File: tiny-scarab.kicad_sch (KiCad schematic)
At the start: 22 parts, among them J1 Conn_02x07_Odd_Even, J2 Conn_01x05_Pin, J4 Conn_02x07_Odd_Even, J5 Screw_Hole, J6 Screw_Hole, J7 Screw_Hole, J8 Screw_Hole, Q3 IRLML2502TRPBF, SW4 SLW-883935-2A-D, SW5 PTS636_SL43_SMTR_LFS, U1 CH32V003F4P6

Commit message: Improve layout
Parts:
- removed J2: Conn_01x05_Pin, Connector_PinHeader_2.54mm:PinHeader_1x05_P2.54mm_Vertical, symbol Connector:Conn_01x05_Pin
- added J2: Conn_01x05_Pin, Tiny_Scarab:PinHeader_1x05_P2.54mm_Vertical, symbol Tiny_Scarab:Conn_01x05_Pin
- Q3: footprint Package_TO_SOT_SMD:SOT-23 -> Tiny_Scarab:SOT-23
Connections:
- net +3V3: now also J2.2 (Pin_2)
- net GND: now also J2.1 (Pin_1)
- net RST_IN: now also J2.5 (Pin_5)
- net SWCLK_IN: now also J2.3 (Pin_3)
- net SWDIO_IN: now also J2.4 (Pin_4)
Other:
- note added: "5mA 1V7 AMBER 732-12014-2-ND"
- note added: "5mA 2V7 GREEN 732-12014-2-ND"
- note added: "5mA 2V9 BLUE 732-12014-2-ND"

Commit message: Improve layout
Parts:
- removed J2: Conn_01x05_Pin, Tiny_Scarab:PinHeader_1x05_P2.54mm_Vertical, symbol Tiny_Scarab:Conn_01x05_Pin
- removed SW4: SLW-883935-2A-D, Tiny_Scarab:SLW-883935-2A-D, symbol Tiny_Scarab:SLW-883935-2A-D
- added C26, C33, C34, C36: 100n, Capacitor_SMD:C_0402_1005Metric_Pad0.74x0.62mm_HandSolder, symbol Device:C
- added C30, C31, C32, C35, C37, C38, C39, C40: 10u, Capacitor_SMD:C_0805_2012Metric, symbol Device:C
- added F2: 0402L050SLKR, Tiny_Scarab:0402L050SLKR, symbol Device:Polyfuse_Small
- added J2: ~, Tiny_Scarab:Tag-Connect_TC2050-IDC-NL_2x05_P1.27mm_Vertical_with_bottom_clip, symbol Tiny_Scarab:TC2050-IDC-NL-WCH-LinkE-R0-1v3
- added R20, R21: 0, Resistor_SMD:R_0402_1005Metric_Pad0.72x0.64mm_HandSolder, symbol Device:R
- added SW6: SLW-883935-2A-D, Tiny_Scarab:SLW-883935-2A-D, symbol Tiny_Scarab:SLW-883935-2A-D
- added TP1, TP2, TP3, TP4, TP5, TP6, TP7: TestPoint, Tiny_Scarab:TestPoint_Pad_D1.0mm, symbol Connector:TestPoint
- C27: renamed from C20; GPN GPC0402104-25 -> (none); MPN (none) -> GPC0402104-25
- C28: renamed from C21; GPN GPC0402104-25 -> (none); MPN (none) -> GPC0402104-25
- C29: renamed from C25; GPN GPC0402104-25 -> (none); MPN (none) -> GPC0402104-25
- C41: renamed from C22; GPN GPC0402220 -> (none); MPN (none) -> GPC0402220; now left out of the parts list
- C42: renamed from C23; GPN GPC0402220 -> (none); MPN (none) -> GPC0402220; now left out of the parts list
- J5, J6, J7, J8: now not fitted; now left out of the parts list
- Q3: DPN IRLML2502TRPBFTR-ND -> (none); Distributor DigiKey -> (none); SPN (none) -> IRLML2502TRPBFTR-ND; Supplier (none) -> DigiKey
- R22: renamed from R21; GPN GPR0402470R -> (none); MPN (none) -> GPR0402470R
- R23: renamed from R13; GPN GPR040210K -> (none); MPN (none) -> GPR040210K
- R24: renamed from R12; GPN GPR04021K -> (none); MPN (none) -> GPR04021K
- R25: renamed from R8; value 470 -> 200; GPN GPR0402470R -> (none); MPN (none) -> GPR0402200R
- U3: renamed from U1; now not fitted; now left out of the parts list
- renumbered J4 to J3, J1 to J4, D7 to LED4, XTAL1 to XTAL2
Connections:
- net +3V3: now also SW6.1 (A), TP3.1
- net +5V: now also J2.1 (5V), SW6.3 (C), TP1.1
- net GND: now also C26.2, C30.2, C31.2, C32.2, C33.2, C34.2, C35.2, C36.2, C37.2, C38.2, C39.2, C40.2, J2.5 (GND), TP2.1
- net RST_IN: now also J2.2 (RST)
- net RST_OUT: now also TP5.1
- net RX: now also R20.1, TP7.1; no longer U3.2 (PD5)
- net SWCLK_IN: now also J2.9 (TCK/SWCLK)
- net SWDIO_IN: now also J2.7 (TMS/SWDIO)
- net SWDIO_OUT: now also TP4.1
- net TX: now also R21.1, TP6.1; no longer U3.3 (PD6)
- net VDD: now also C26.1, C30.1, C31.1, C32.1, C33.1, C34.1, C35.1, C36.1, C37.1, C38.1, C39.1, C40.1, F2.2
- new net: F2.1, SW6.2 (B)
- new net: R20.2, U3.2 (PD5)
- new net: R21.2, U3.3 (PD6)
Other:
- note added: "10mA 3V GREEN"
- note added: "Test Pads"
- note added: "The CH32V003F4P6 target is powered with 3V3 or 5V, depending on the state of SW4."
- note added: "These Test Pads are located between the flash/debug probe and target MCU."
- note removed: "5mA 1V7 AMBER 732-12014-2-ND"
- note removed: "5mA 2V7 GREEN"
- note removed: "5mA 2V7 GREEN 732-12014-2-ND"
- note removed: "5mA 2V9 BLUE 732-12014-2-ND"
- note removed: "The CH32V003F4P6 target MCU is supplied either 3V3 or 5V power, depending on the state of SW4."
- moved on the sheet: C27, C28, C29, C41, C42, J3, J4, R22, R23, SW5, XTAL2

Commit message: Update design
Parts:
- removed R20, R21: 0, Resistor_SMD:R_0402_1005Metric_Pad0.72x0.64mm_HandSolder, symbol Device:R
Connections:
- net RX: now also U3.2 (PD5)
- net TX: now also U3.3 (PD6)
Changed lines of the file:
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@@
-    (stroke (width 0) (type default))
-  )
-  (wire (pts (xy 123.19 49.53) (xy 129.54 49.53))
     (stroke (width 0) (type default))
   )
@@
     (stroke (width 0) (type dash))
   )
+  (wire (pts (xy 115.57 52.07) (xy 127 52.07))
+    (stroke (width 0) (type default))
+  )
   (wire (pts (xy 167.64 29.21) (xy 172.72 29.21))
     (stroke (width 0) (type default))
@@
     (stroke (width 0) (type default))
   )
-  (wire (pts (xy 115.57 55.88) (xy 125.73 55.88))
+  (wire (pts (xy 115.57 54.61) (xy 127 54.61))
     (stroke (width 0) (type default))
   )
@@
     (stroke (width 0) (type default))
   )
-  (wire (pts (xy 115.57 55.88) (xy 115.57 54.61))
+  (wire (pts (xy 115.57 49.53) (xy 127 49.53))
     (stroke (width 0) (type default))
   )
@@
     (stroke (width 0) (type default))
   )
-  (wire (pts (xy 123.19 52.07) (xy 129.54 52.07))
-    (stroke (width 0) (type default))
-  )
   (wire (pts (xy 185.42 93.98) (xy 190.5 93.98))
     (stroke (width 0) (type default))
@@
     (effects (font (size 1.27 1.27)) (justify left bottom))
   )
-  (label "RX" (at 129.54 49.53 180) (fields_autoplaced)
-    (effects (font (size 1.27 1.27)) (justify right bottom))
-  )
-  (label "RST_OUT" (at 125.73 55.88 180) (fields_autoplaced)
+  (label "RX" (at 127 49.53 180) (fields_autoplaced)
+    (effects (font (size 1.27 1.27)) (justify right bottom))
+  )
+  (label "RST_OUT" (at 127 54.61 180) (fields_autoplaced)
     (effects (font (size 1.27 1.27)) (justify right bottom))
   )
@@
     (effects (font (size 1.27 1.27)) (justify right bottom))
   )
-  (label "TX" (at 129.54 52.07 180) (fields_autoplaced)
+  (label "TX" (at 127 52.07 180) (fields_autoplaced)
     (effects (font (size 1.27 1.27)) (justify right bottom))
   )
@@
     )
   )
-  (symbol (lib_id "Device:R") (at 119.38 49.53 270) (unit 1)
-    (in_bom yes) (on_board yes) (dnp no)
-    (property "Reference" "R20" (at 119.38 49.53 90)
-      (effects (font (size 1.27 1.27)))
-    )
-    (property "Value" "0" (at 123.19 48.26 90)
-      (effects (font (size 1.27 1.27)))
-    )
-    (property "Footprint" "Resistor_SMD:R_0402_1005Metric_Pad0.72x0.64mm_HandSolder" (at 119.38 47.752 90)
-      (effects (font (size 1.27 1.27)) hide)
-    )
-    (property "Datasheet" "~" (at 119.38 49.53 0)
-      (effects (font (size 1.27 1.27)) hide)
-    )
-    (property "MPN" "GPR02010R" (at 119.38 49.53 0)
-      (effects (font (size 1.27 1.27)) hide)
-    )
-    (pin "2")
-    (pin "1")
-    (instances
-      (project "tiny-scarab"
-        (path "/156c5422-ee07-49a4-8263-a2dbd26b90bd"
-          (reference "R20") (unit 1)
-        )
-      )
-    )
-  )
   (symbol (lib_id "Connector:TestPoint") (at 101.6 95.25 90) (unit 1)
     (in_bom no) (on_board yes) (dnp yes)
@@
         )
       )
-    )
-  )
-  (symbol (lib_id "Device:R") (at 119.38 52.07 270) (unit 1)
-    (in_bom yes) (on_board yes) (dnp no)
-    (property "Reference" "R21" (at 119.38 52.07 90)
-      (effects (font (size 1.27 1.27)))
-    )
-    (property "Value" "0" (at 123.19 50.8 90)
-      (effects (font (size 1.27 1.27)))
-    )
-    (property "Footprint" "Resistor_SMD:R_0402_1005Metric_Pad0.72x0.64mm_HandSolder" (at 119.38 50.292 90)
-      (effects (font (size 1.27 1.27)) hide)
-    )
-    (property "Datasheet" "~" (at 119.38 52.07 0)
-      (effects (font (size 1.27 1.27)) hide)
-    )
-    (property "MPN" "GPR02010R" (at 119.38 52.07 0)
-      (effects (font (size 1.27 1.27)) hide)
-    )
-    (pin "2")
-    (pin "1")
-    (instances
-      (project "tiny-scarab"
-        (path "/156c5422-ee07-49a4-8263-a2dbd26b90bd"
-          (reference "R21") (unit 1)
-        )
-      )

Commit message: Update layout
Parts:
- F2: value 0402L050SLKR -> ~
- LED4: value LED -> ~
- Q3: value IRLML2502TRPBF -> ~
- SW4: renamed from SW5; value PTS636_SL43_SMTR_LFS -> ~
- SW5: renamed from SW6; value SLW-883935-2A-D -> ~
- U3: value CH32V003F4P6 -> ~; MPN (none) -> CH32V003F4P6; Manufacturer (none) -> WCH; SPN (none) -> 1005005036714708; Supplier (none) -> AliExpress; now fitted; now in the parts list
- XTAL2: value ECS-240-20-30B-TR -> (none)

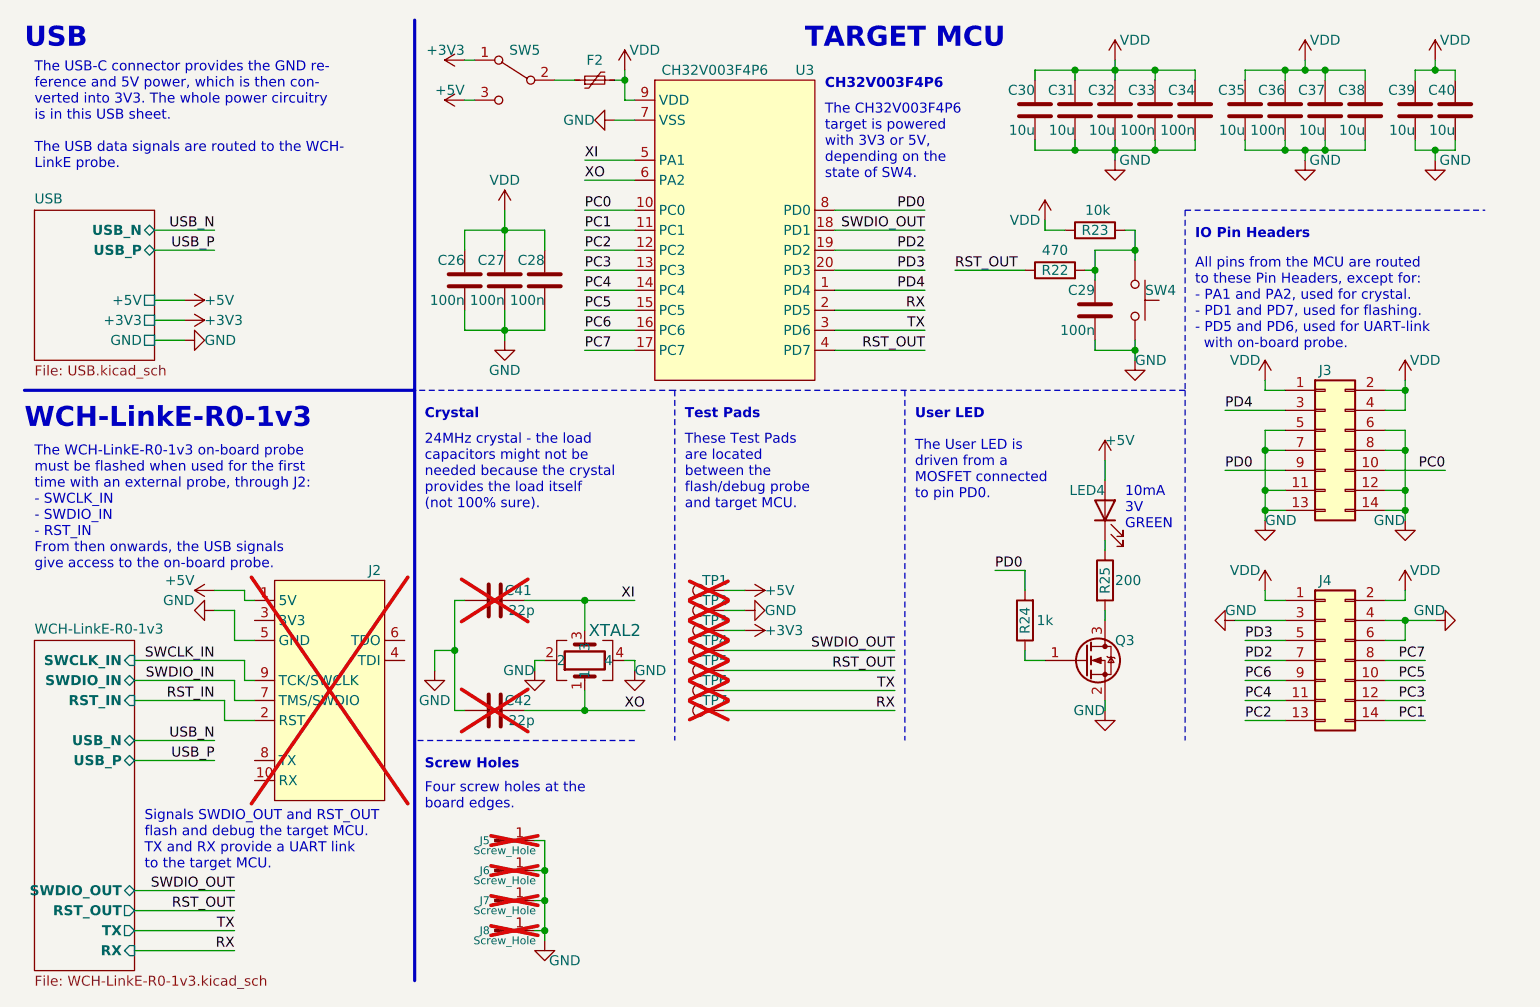
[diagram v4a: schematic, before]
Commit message: Prepare PCB for JLCPCB production
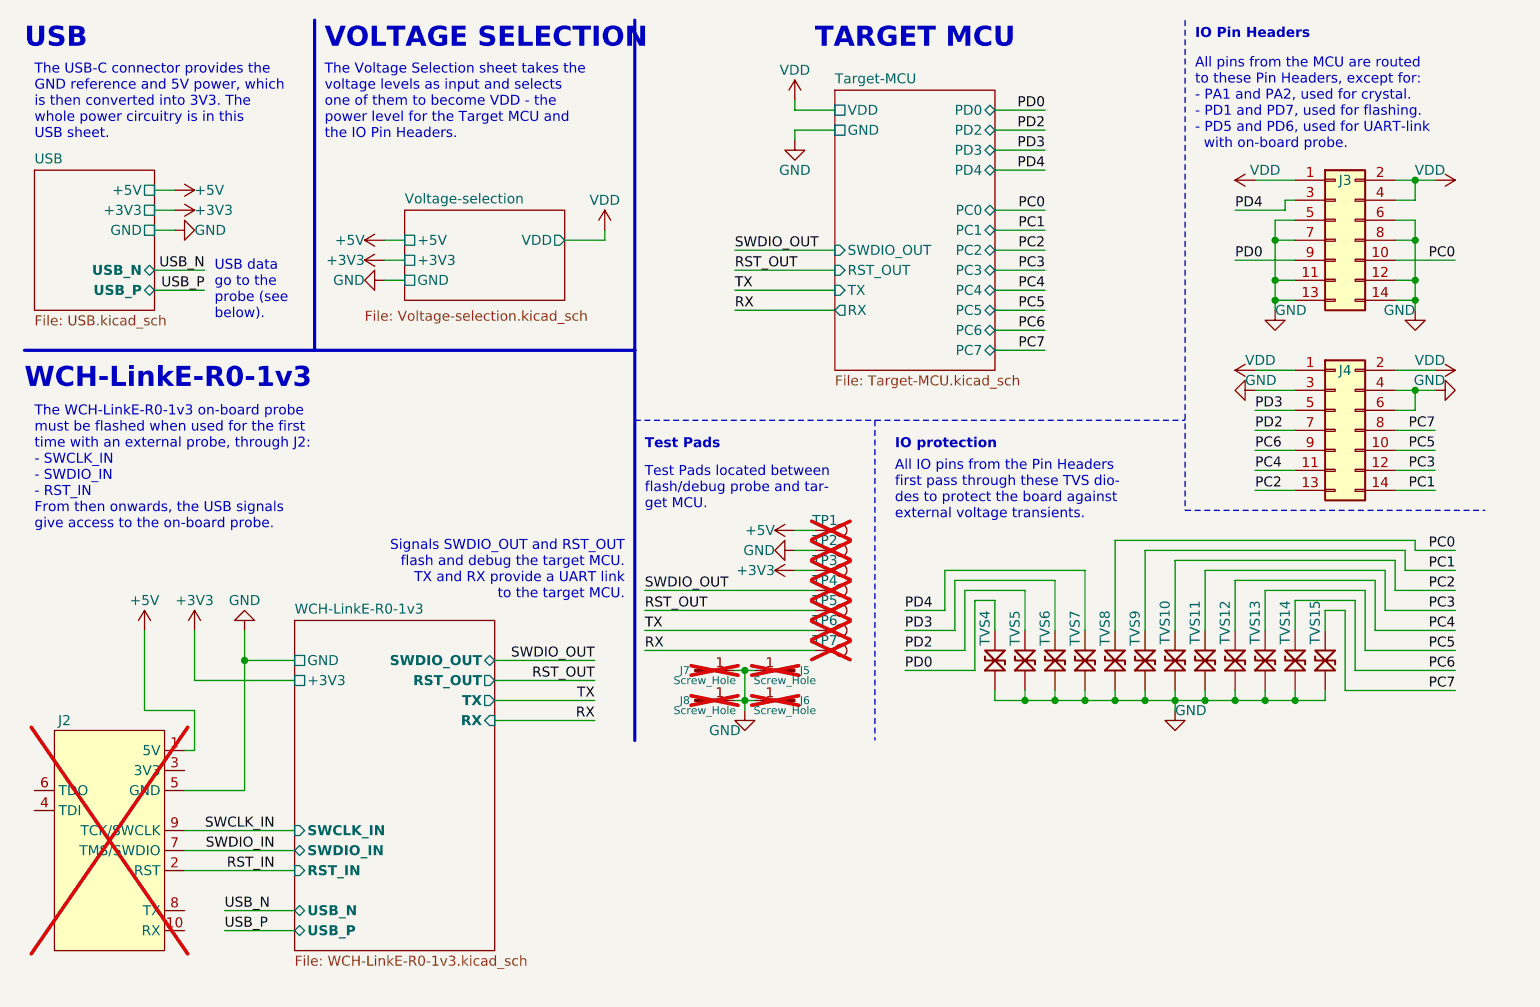
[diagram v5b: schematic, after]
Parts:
- removed C26, C27, C28, C29, C33, C34, C36: 100n, Capacitor_SMD:C_0402_1005Metric_Pad0.74x0.62mm_HandSolder, symbol Device:C
- removed C30, C31, C32, C35, C37, C38, C39, C40: 10u, Capacitor_SMD:C_0805_2012Metric, symbol Device:C
- removed C41, C42: 22p, Capacitor_SMD:C_0402_1005Metric_Pad0.74x0.62mm_HandSolder, symbol Device:C
- removed F2: ~, Tiny_Scarab:0402L050SLKR, symbol Device:Polyfuse_Small
- removed LED4: ~, LED_SMD:LED_0603_1608Metric_Pad1.05x0.95mm_HandSolder, symbol Device:LED
- removed Q3: ~, Tiny_Scarab:SOT-23, symbol Tiny_Scarab:IRLML2502TRPBF
- removed R22: 470, Resistor_SMD:R_0402_1005Metric_Pad0.72x0.64mm_HandSolder, symbol Device:R
- removed R23: 10k, Resistor_SMD:R_0402_1005Metric_Pad0.72x0.64mm_HandSolder, symbol Device:R
- removed R24: 1k, Resistor_SMD:R_0402_1005Metric_Pad0.72x0.64mm_HandSolder, symbol Device:R
- removed R25: 200, Resistor_SMD:R_0402_1005Metric_Pad0.72x0.64mm_HandSolder, symbol Device:R
- removed SW4: ~, Tiny_Scarab:SW_Tactile_SPST_NO_Straight_CK_PTS636Sx43SMTRLFS, symbol Tiny_Scarab:PTS636_SL43_SMTR_LFS
- removed SW5: ~, Tiny_Scarab:SLW-883935-2A-D, symbol Tiny_Scarab:SLW-883935-2A-D
- removed U3: ~, Package_SO:TSSOP-20_4.4x6.5mm_P0.65mm, symbol Tiny_Scarab:CH32V003F4P6
- removed XTAL2: (no value), Tiny_Scarab:CRYSTAL4_ECS-240-20-30B-TR_ECS, symbol Tiny_Scarab:ECS-240-20-30B-TR
- added TVS10, TVS11, TVS12, TVS13, TVS14, TVS15, TVS4, TVS5, TVS6, TVS7, TVS8, TVS9: 5V, Tiny_Scarab:D_SOD-323_CDSOD323-T05LC, symbol Tiny_Scarab:CDSOD323-T05LC
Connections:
- net GND: now also TVS10.2, TVS11.2, TVS12.2, TVS13.2, TVS14.2, TVS15.2, TVS4.2, TVS5.2, TVS6.2, TVS7.2, TVS8.2, TVS9.2
- net PC0: now also TVS8.1
- net PC1: now also TVS9.1
- net PC2: now also TVS10.1
- net PC3: now also TVS11.1
- net PC4: now also TVS12.1
- net PC5: now also TVS13.1
- net PC6: now also TVS14.1
- net PC7: now also TVS15.1
- net PD0: now also TVS4.1
- net PD2: now also TVS5.1
- net PD3: now also TVS6.1
- net PD4: now also TVS7.1
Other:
- added sheet Target-MCU (Target-MCU.kicad_sch)
- added sheet Voltage-selection (Voltage-selection.kicad_sch)
- sheet WCH-LinkE-R0-1v3 ports: added +3V3, GND; removed none
- note added: "All IO pins from the Pin Headers first pass through these TVS dio- des to protect the board against external voltage transients."
- note added: "IO protection"
- note added: "Test Pads located between flash/debug probe and tar- get MCU."
- note added: "The USB-C connector provides the GND reference and 5V power, which is then converted into 3V3. The whole power circuitry is in this USB sheet."
- note added: "The Voltage Selection sheet takes the voltage levels as input and selects one of them to become VDD - the power level for the Target MCU and the IO Pin Headers."
- note added: "USB data go to the probe (see below)."
- note added: "VOLTAGE SELECTION"
- note removed: "10mA 3V GREEN"
- note removed: "24MHz crystal - the load capacitors might not be needed because the crystal provides the load itself (not 100% sure)."
- note removed: "CH32V003F4P6"
- note removed: "Crystal"
- note removed: "Four screw holes at the board edges."
- note removed: "Screw Holes"
- note removed: "The CH32V003F4P6 target is powered with 3V3 or 5V, depending on the state of SW4."
- note removed: "The USB-C connector provides the GND re- ference and 5V power, which is then con- verted into 3V3. The whole power circuitry is in this USB sheet. The USB data signals are routed to the WCH- LinkE probe."
- note removed: "The User LED is driven from a MOSFET connected to pin PD0."
- note removed: "These Test Pads are located between the flash/debug probe and target MCU."
- note removed: "User LED"
- moved on the sheet: J2, J5, J6, J7, J8

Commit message: Renumber designators and draw new silkscreen
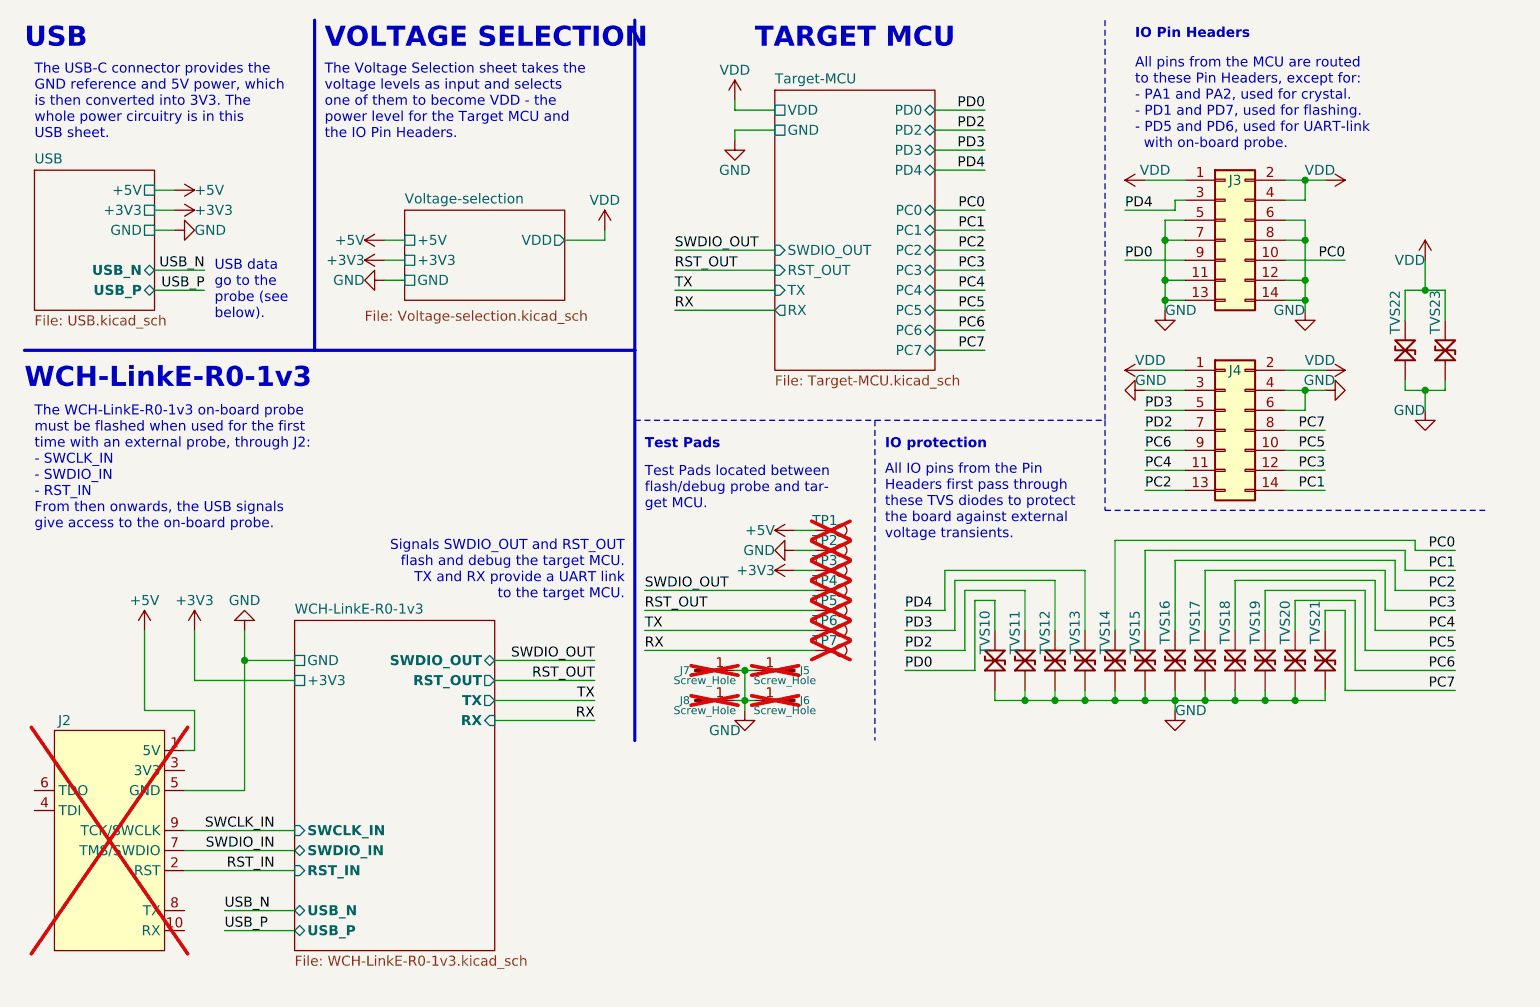
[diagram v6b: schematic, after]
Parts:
- added TVS22, TVS23: 5V, Tiny_Scarab:D_SOD-323_CDSOD323-T05LC, symbol Tiny_Scarab:CDSOD323-T05LC
- renumbered TVS4 to TVS10, TVS5 to TVS11, TVS6 to TVS12, TVS7 to TVS13, TVS8 to TVS14, TVS9 to TVS15, TVS10 to TVS16, TVS11 to TVS17, TVS12 to TVS18, TVS13 to TVS19, TVS14 to TVS20, TVS15 to TVS21
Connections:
- net GND: now also TVS22.2, TVS23.2
- net VDD: now also TVS22.1, TVS23.1
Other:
- note added: "All IO pins from the Pin Headers first pass through these TVS diodes to protect the board against external voltage transients."
- note removed: "All IO pins from the Pin Headers first pass through these TVS dio- des to protect the board against external voltage transients."
- moved on the sheet: J3, J4
